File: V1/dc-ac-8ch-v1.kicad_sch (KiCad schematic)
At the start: 102 parts, among them J1 DB142V-5.08-4P, J2 DB142V-5.08-4P, J3 DB142V-5.08-2P, J4 DB142V-5.08-4P, J5 DB142V-5.08-4P, J6 DB142V-5.08-2P, U1 MOC3063S, U2 MOC3063S, U3 MOC3063S, U4 MOC3063S, U5 MOC3063S, U6 MOC3063S, U7 MOC3063S, U8 MOC3063S

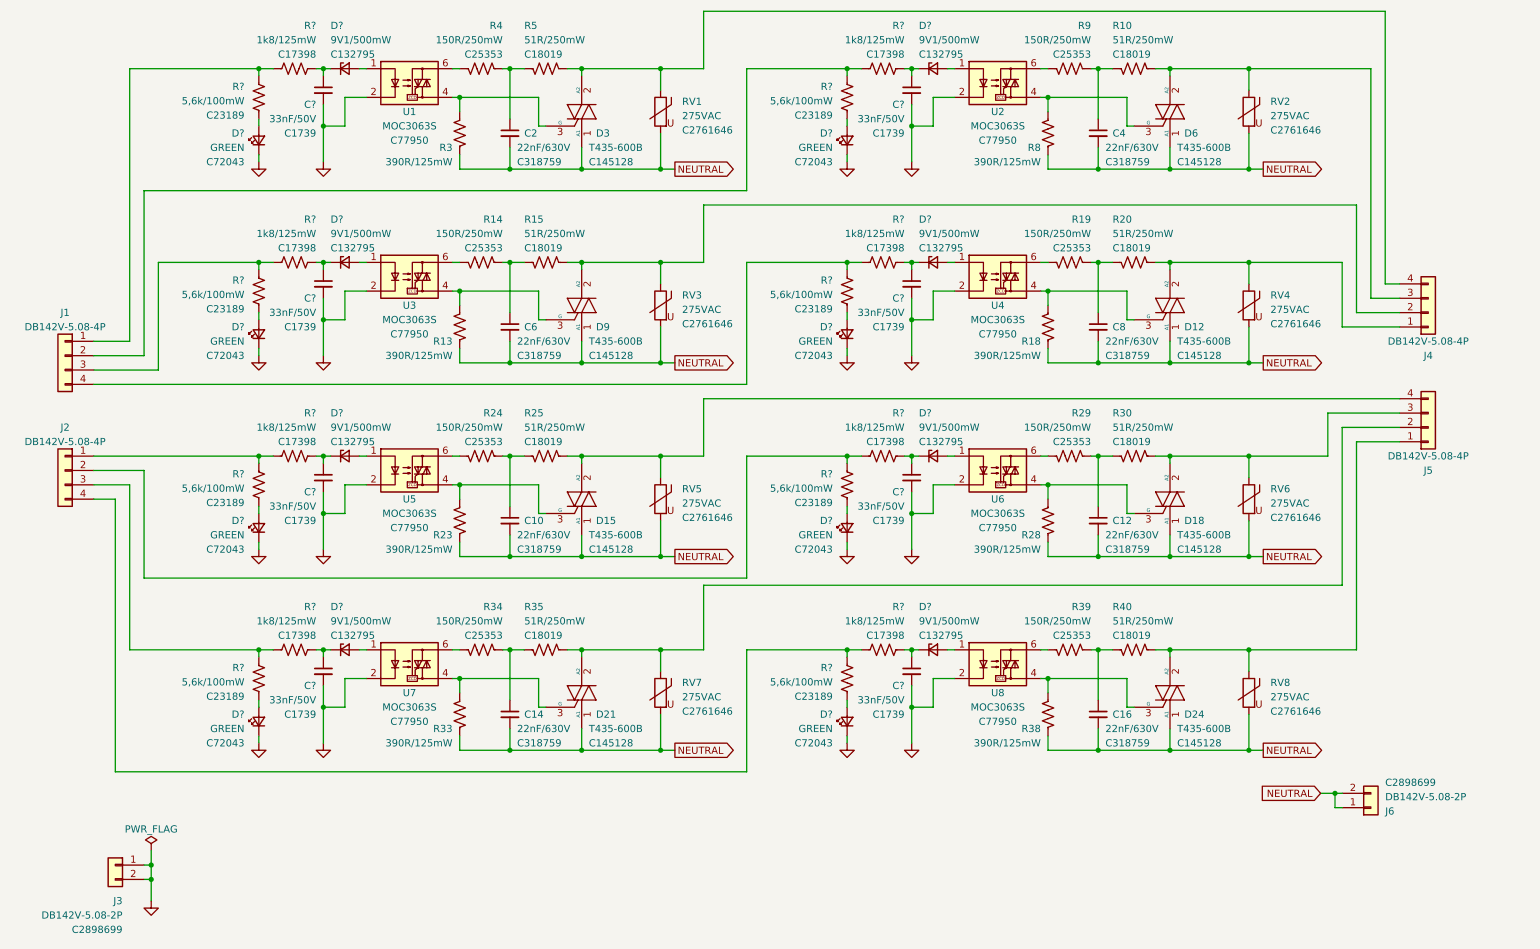
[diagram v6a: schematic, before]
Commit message: Layout redone, footprints updated
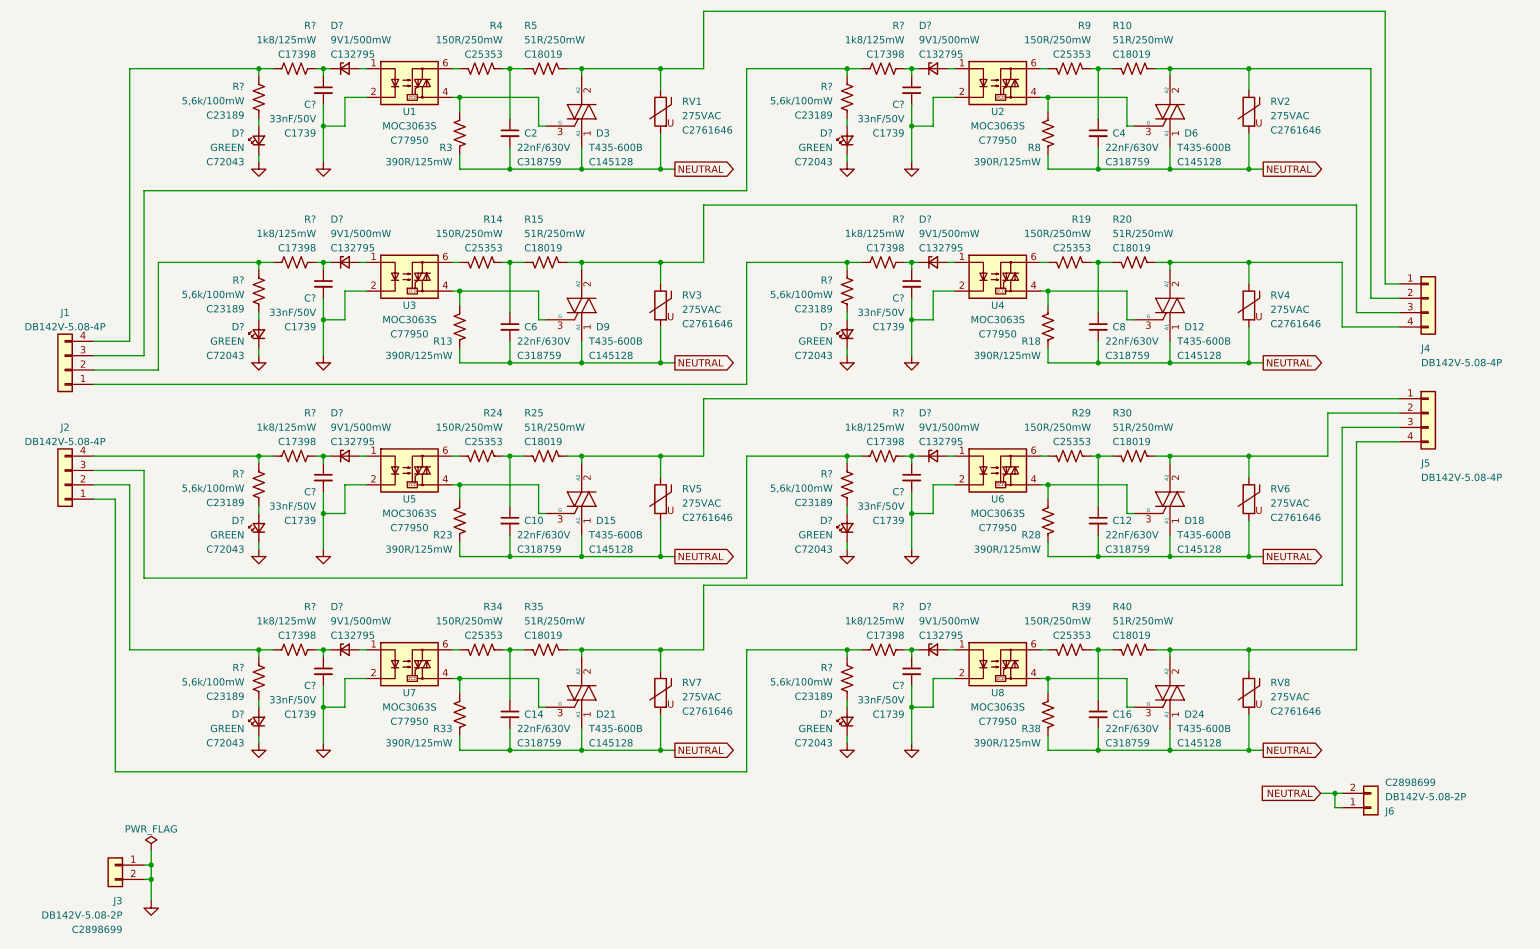
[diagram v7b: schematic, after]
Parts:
- J1, J2, J4, J5: footprint Tales:TerminalBlock_Dibo_DB142V-5.08-4P_1x04_P5.08mm_Vertical_copy -> Tales:TerminalBlock_Dibo_DB142V-5.08-4P_1x04_P5.08mm_Vertical
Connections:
- net at D21.2 (A2), R35.1, RV7.1: now also J5.3 (Pin_3); no longer J5.2 (Pin_2)
- net at D12.2 (A2), R20.1, RV4.1: now also J4.4 (Pin_4); no longer J4.1 (Pin_1)
- net at R?.1, R?.2: now also J2.1 (Pin_1); no longer J2.4 (Pin_4)
- net at D3.2 (A2), R5.1, RV1.1: now also J4.1 (Pin_1); no longer J4.4 (Pin_4)
- net at D9.2 (A2), R15.1, RV3.1: now also J4.3 (Pin_3); no longer J4.2 (Pin_2)
- net at D15.2 (A2), R25.1, RV5.1: now also J5.1 (Pin_1); no longer J5.4 (Pin_4)
- net at R?.1, R?.2: now also J1.4 (Pin_4); no longer J1.1 (Pin_1)
- net at R?.1, R?.2: now also J2.4 (Pin_4); no longer J2.1 (Pin_1)
- net at R?.1, R?.2: now also J1.1 (Pin_1); no longer J1.4 (Pin_4)
- net at R?.1, R?.2: now also J1.2 (Pin_2); no longer J1.3 (Pin_3)
- net at D18.2 (A2), R30.1, RV6.1: now also J5.2 (Pin_2); no longer J5.3 (Pin_3)
- net at D6.2 (A2), R10.1, RV2.1: now also J4.2 (Pin_2); no longer J4.3 (Pin_3)
- net at R?.1, R?.2: now also J1.3 (Pin_3); no longer J1.2 (Pin_2)
- net at R?.1, R?.2: now also J2.2 (Pin_2); no longer J2.3 (Pin_3)
- net at R?.1, R?.2: now also J2.3 (Pin_3); no longer J2.2 (Pin_2)
- net at D24.2 (A2), R40.1, RV8.1: now also J5.4 (Pin_4); no longer J5.1 (Pin_1)
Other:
- moved on the sheet: J1, J2
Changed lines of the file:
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@@
     )
   )
-  (symbol (lib_id "Connector_Generic:Conn_01x04") (at 266.7 72.39 0) (mirror x) (unit 1)
+  (symbol (lib_id "Connector_Generic:Conn_01x04") (at 266.7 69.85 0) (unit 1)
     (in_bom yes) (on_board yes) (dnp no)
-    (property "Reference" "J4" (at 266.7 80.01 0)
-      (effects (font (size 1.27 1.27)))
+    (property "Reference" "J4" (at 265.43 78.74 0)
+      (effects (font (size 1.27 1.27)) (justify left))
     )
-    (property "Value" "DB142V-5.08-4P" (at 266.7 77.47 0)
-      (effects (font (size 1.27 1.27)))
+    (property "Value" "DB142V-5.08-4P" (at 265.43 81.28 0)
+      (effects (font (size 1.27 1.27)) (justify left))
     )
-    (property "Footprint" "Tales:TerminalBlock_Dibo_DB142V-5.08-4P_1x04_P5.08mm_Vertical_copy" (at 266.7 72.39 0)
+    (property "Footprint" "Tales:TerminalBlock_Dibo_DB142V-5.08-4P_1x04_P5.08mm_Vertical" (at 266.7 69.85 0)
       (effects (font (size 1.27 1.27)) hide)
     )
-    (property "Datasheet" "~" (at 266.7 72.39 0)
+    (property "Datasheet" "~" (at 266.7 69.85 0)
       (effects (font (size 1.27 1.27)) hide)
     )
@@
     )
   )
-  (symbol (lib_id "Connector_Generic:Conn_01x04") (at 266.7 92.71 0) (mirror x) (unit 1)
+  (symbol (lib_id "Connector_Generic:Conn_01x04") (at 266.7 90.17 0) (unit 1)
     (in_bom yes) (on_board yes) (dnp no)
-    (property "Reference" "J5" (at 266.7 100.33 0)
-      (effects (font (size 1.27 1.27)))
+    (property "Reference" "J5" (at 265.43 99.06 0)
+      (effects (font (size 1.27 1.27)) (justify left))
     )
-    (property "Value" "DB142V-5.08-4P" (at 266.7 97.79 0)
-      (effects (font (size 1.27 1.27)))
+    (property "Value" "DB142V-5.08-4P" (at 265.43 101.6 0)
+      (effects (font (size 1.27 1.27)) (justify left))
     )
-    (property "Footprint" "Tales:TerminalBlock_Dibo_DB142V-5.08-4P_1x04_P5.08mm_Vertical_copy" (at 266.7 92.71 0)
+    (property "Footprint" "Tales:TerminalBlock_Dibo_DB142V-5.08-4P_1x04_P5.08mm_Vertical" (at 266.7 90.17 0)
       (effects (font (size 1.27 1.27)) hide)
     )
-    (property "Datasheet" "~" (at 266.7 92.71 0)
+    (property "Datasheet" "~" (at 266.7 90.17 0)
       (effects (font (size 1.27 1.27)) hide)
     )
@@
     )
   )
-  (symbol (lib_id "Connector_Generic:Conn_01x04") (at 25.4 100.33 0) (mirror y) (unit 1)
+  (symbol (lib_id "Connector_Generic:Conn_01x04") (at 25.4 102.87 180) (unit 1)
     (in_bom yes) (on_board yes) (dnp no) (fields_autoplaced)
     (property "Reference" "J2" (at 25.4 92.71 0)
@@
       (effects (font (size 1.27 1.27)))
     )
-    (property "Footprint" "Tales:TerminalBlock_Dibo_DB142V-5.08-4P_1x04_P5.08mm_Vertical_copy" (at 25.4 100.33 0)
+    (property "Footprint" "Tales:TerminalBlock_Dibo_DB142V-5.08-4P_1x04_P5.08mm_Vertical" (at 25.4 102.87 0)
       (effects (font (size 1.27 1.27)) hide)
     )
-    (property "Datasheet" "~" (at 25.4 100.33 0)
+    (property "Datasheet" "~" (at 25.4 102.87 0)
       (effects (font (size 1.27 1.27)) hide)
     )
@@
     )
   )
-  (symbol (lib_id "Connector_Generic:Conn_01x04") (at 25.4 80.01 0) (mirror y) (unit 1)
+  (symbol (lib_id "Connector_Generic:Conn_01x04") (at 25.4 82.55 180) (unit 1)
     (in_bom yes) (on_board yes) (dnp no) (fields_autoplaced)
     (property "Reference" "J1" (at 25.4 72.39 0)
@@
       (effects (font (size 1.27 1.27)))
     )
-    (property "Footprint" "Tales:TerminalBlock_Dibo_DB142V-5.08-4P_1x04_P5.08mm_Vertical_copy" (at 25.4 80.01 0)
+    (property "Footprint" "Tales:TerminalBlock_Dibo_DB142V-5.08-4P_1x04_P5.08mm_Vertical" (at 25.4 82.55 0)
       (effects (font (size 1.27 1.27)) hide)
     )
-    (property "Datasheet" "~" (at 25.4 80.01 0)
+    (property "Datasheet" "~" (at 25.4 82.55 0)
       (effects (font (size 1.27 1.27)) hide)
     )

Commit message: Repo cleanup
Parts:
- J1, J2, J4, J5: JLCPCB BOM (none) -> 1; LCSC Part # (none) -> C2898701; Mfr (none) -> DIBO; Mfr Part # (none) -> DB142V-5.08-4P; Package (none) -> 01X04 P5.08; Technology (none) -> Spring Cage; Vendor (none) -> JLCPCB; Vendor Part # (none) -> C2898701
- J3, J6: Package 01x08 P5.08 -> 01x02 P5.08
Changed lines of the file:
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@@
       (effects (font (size 1.27 1.27)) hide)
     )
-    (property "Package" "01x08 P5.08" (at 256.54 160.02 0)
+    (property "Package" "01x02 P5.08" (at 256.54 160.02 0)
       (effects (font (size 1.27 1.27)) hide)
     )
@@
       (effects (font (size 1.27 1.27)) hide)
     )
+    (property "JLCPCB BOM" "1" (at 266.7 69.85 0)
+      (effects (font (size 1.27 1.27)) hide)
+    )
+    (property "LCSC Part #" "C2898701" (at 266.7 69.85 0)
+      (effects (font (size 1.27 1.27)) hide)
+    )
+    (property "Mfr" "DIBO" (at 266.7 69.85 0)
+      (effects (font (size 1.27 1.27)) hide)
+    )
+    (property "Mfr Part #" "DB142V-5.08-4P" (at 266.7 69.85 0)
+      (effects (font (size 1.27 1.27)) hide)
+    )
+    (property "Package" "01X04 P5.08" (at 266.7 69.85 0)
+      (effects (font (size 1.27 1.27)) hide)
+    )
+    (property "Technology" "Spring Cage" (at 266.7 69.85 0)
+      (effects (font (size 1.27 1.27)) hide)
+    )
+    (property "Vendor" "JLCPCB" (at 266.7 69.85 0)
+      (effects (font (size 1.27 1.27)) hide)
+    )
+    (property "Vendor Part #" "C2898701" (at 266.7 69.85 0)
+      (effects (font (size 1.27 1.27)) hide)
+    )
     (pin "1")
     (pin "2")
@@
       (effects (font (size 1.27 1.27)) hide)
     )
+    (property "JLCPCB BOM" "1" (at 266.7 90.17 0)
+      (effects (font (size 1.27 1.27)) hide)
+    )
+    (property "LCSC Part #" "C2898701" (at 266.7 90.17 0)
+      (effects (font (size 1.27 1.27)) hide)
+    )
+    (property "Mfr" "DIBO" (at 266.7 90.17 0)
+      (effects (font (size 1.27 1.27)) hide)
+    )
+    (property "Mfr Part #" "DB142V-5.08-4P" (at 266.7 90.17 0)
+      (effects (font (size 1.27 1.27)) hide)
+    )
+    (property "Package" "01X04 P5.08" (at 266.7 90.17 0)
+      (effects (font (size 1.27 1.27)) hide)
+    )
+    (property "Technology" "Spring Cage" (at 266.7 90.17 0)
+      (effects (font (size 1.27 1.27)) hide)
+    )
+    (property "Vendor" "JLCPCB" (at 266.7 90.17 0)
+      (effects (font (size 1.27 1.27)) hide)
+    )
+    (property "Vendor Part #" "C2898701" (at 266.7 90.17 0)
+      (effects (font (size 1.27 1.27)) hide)
+    )
     (pin "1")
     (pin "2")
@@
       (effects (font (size 1.27 1.27)) hide)
     )
+    (property "JLCPCB BOM" "1" (at 25.4 102.87 0)
+      (effects (font (size 1.27 1.27)) hide)
+    )
+    (property "LCSC Part #" "C2898701" (at 25.4 102.87 0)
+      (effects (font (size 1.27 1.27)) hide)
+    )
+    (property "Mfr" "DIBO" (at 25.4 102.87 0)
+      (effects (font (size 1.27 1.27)) hide)
+    )
+    (property "Mfr Part #" "DB142V-5.08-4P" (at 25.4 102.87 0)
+      (effects (font (size 1.27 1.27)) hide)
+    )
+    (property "Package" "01X04 P5.08" (at 25.4 102.87 0)
+      (effects (font (size 1.27 1.27)) hide)
+    )
+    (property "Technology" "Spring Cage" (at 25.4 102.87 0)
+      (effects (font (size 1.27 1.27)) hide)
+    )
+    (property "Vendor" "JLCPCB" (at 25.4 102.87 0)
+      (effects (font (size 1.27 1.27)) hide)
+    )
+    (property "Vendor Part #" "C2898701" (at 25.4 102.87 0)
+      (effects (font (size 1.27 1.27)) hide)
+    )
     (pin "1")
     (pin "2")
@@
       (effects (font (size 1.27 1.27)) hide)
     )
-    (property "Package" "01x08 P5.08" (at 34.29 170.18 0)
+    (property "Package" "01x02 P5.08" (at 34.29 170.18 0)
       (effects (font (size 1.27 1.27)) hide)
     )
@@
       (effects (font (size 1.27 1.27)) hide)
     )
+    (property "JLCPCB BOM" "1" (at 25.4 82.55 0)
+      (effects (font (size 1.27 1.27)) hide)
+    )
+    (property "LCSC Part #" "C2898701" (at 25.4 82.55 0)
+      (effects (font (size 1.27 1.27)) hide)
+    )
+    (property "Mfr" "DIBO" (at 25.4 82.55 0)
+      (effects (font (size 1.27 1.27)) hide)
+    )
+    (property "Mfr Part #" "DB142V-5.08-4P" (at 25.4 82.55 0)
+      (effects (font (size 1.27 1.27)) hide)
+    )
+    (property "Package" "01X04 P5.08" (at 25.4 82.55 0)
+      (effects (font (size 1.27 1.27)) hide)
+    )
+    (property "Technology" "Spring Cage" (at 25.4 82.55 0)
+      (effects (font (size 1.27 1.27)) hide)
+    )
+    (property "Vendor" "JLCPCB" (at 25.4 82.55 0)
+      (effects (font (size 1.27 1.27)) hide)
+    )
+    (property "Vendor Part #" "C2898701" (at 25.4 82.55 0)
+      (effects (font (size 1.27 1.27)) hide)
+    )
